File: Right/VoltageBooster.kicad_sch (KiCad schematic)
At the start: 5 parts, among them U32 BL8530_501SM

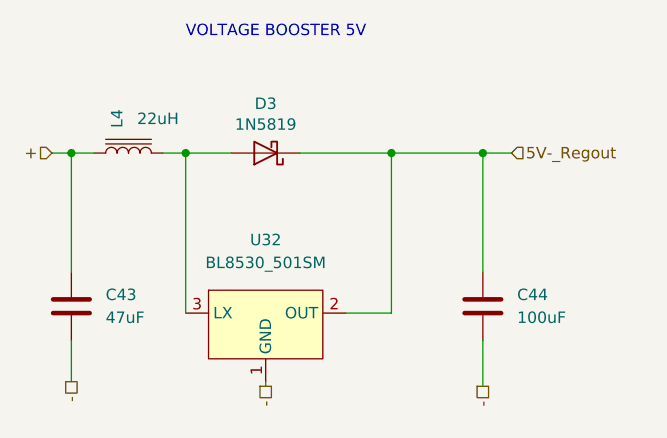
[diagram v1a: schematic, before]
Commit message: upgraded files to kicad7
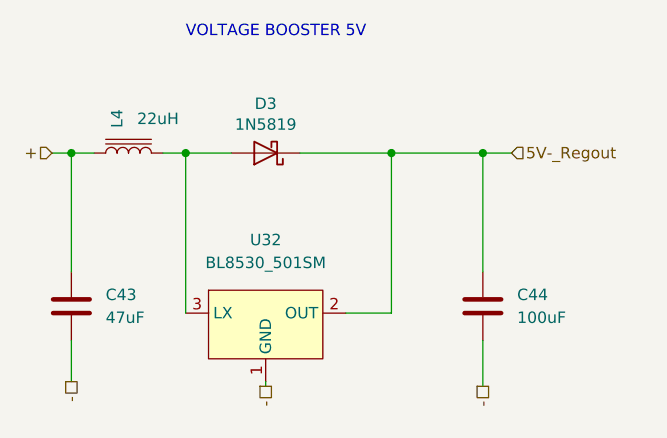
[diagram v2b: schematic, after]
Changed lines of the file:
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@@
-(kicad_sch (version 20211123) (generator eeschema)
+(kicad_sch (version 20230121) (generator eeschema)
   (paper "A4")
   (junction (at 121.158 95.504) (diameter 0) (color 0 0 0 0)
@@
   )
   (wire (pts (xy 154.178 121.412) (xy 154.178 116.332))
-    (stroke (width 0) (type default) (color 0 0 0 0))
+    (stroke (width 0) (type default))
   )
   (wire (pts (xy 121.158 95.504) (xy 126.238 95.504))
-    (stroke (width 0) (type default) (color 0 0 0 0))
+    (stroke (width 0) (type default))
   )
   (wire (pts (xy 108.458 95.504) (xy 110.998 95.504))
-    (stroke (width 0) (type default) (color 0 0 0 0))
+    (stroke (width 0) (type default))
   )
   (wire (pts (xy 154.178 95.504) (xy 144.018 95.504))
-    (stroke (width 0) (type default) (color 0 0 0 0))
+    (stroke (width 0) (type default))
   )
   (wire (pts (xy 106.299 95.504) (xy 108.458 95.504))
-    (stroke (width 0) (type default) (color 0 0 0 0))
+    (stroke (width 0) (type default))
   )
   (wire (pts (xy 144.018 113.284) (xy 144.018 95.504))
-    (stroke (width 0) (type default) (color 0 0 0 0))
+    (stroke (width 0) (type default))
   )
   (wire (pts (xy 108.458 95.504) (xy 108.458 108.712))
-    (stroke (width 0) (type default) (color 0 0 0 0))
+    (stroke (width 0) (type default))
   )
   (wire (pts (xy 154.178 95.504) (xy 154.178 108.712))
-    (stroke (width 0) (type default) (color 0 0 0 0))
+    (stroke (width 0) (type default))
   )
   (wire (pts (xy 130.048 121.412) (xy 130.048 120.904))
-    (stroke (width 0) (type default) (color 0 0 0 0))
+    (stroke (width 0) (type default))
   )
   (wire (pts (xy 144.018 95.504) (xy 133.858 95.504))
-    (stroke (width 0) (type default) (color 0 0 0 0))
+    (stroke (width 0) (type default))
   )
   (wire (pts (xy 154.178 95.504) (xy 157.353 95.504))
-    (stroke (width 0) (type default) (color 0 0 0 0))
+    (stroke (width 0) (type default))
   )
   (wire (pts (xy 118.618 95.504) (xy 121.158 95.504))
-    (stroke (width 0) (type default) (color 0 0 0 0))
+    (stroke (width 0) (type default))
   )
   (wire (pts (xy 138.938 113.284) (xy 144.018 113.284))
-    (stroke (width 0) (type default) (color 0 0 0 0))
+    (stroke (width 0) (type default))
   )
   (wire (pts (xy 121.158 95.504) (xy 121.158 113.284))
-    (stroke (width 0) (type default) (color 0 0 0 0))
+    (stroke (width 0) (type default))
   )
   (wire (pts (xy 108.458 120.904) (xy 108.458 116.332))
-    (stroke (width 0) (type default) (color 0 0 0 0))
+    (stroke (width 0) (type default))
   )
   (text "VOLTAGE BOOSTER 5V" (at 121.158 82.804 0)
     (effects (font (size 1.27 1.27)) (justify left bottom))
   )
-  (hierarchical_label "-" (shape passive) (at 130.048 121.412 270)
+  (hierarchical_label "-" (shape passive) (at 130.048 121.412 270) (fields_autoplaced)
     (effects (font (size 1.27 1.27)) (justify right))
   )
-  (hierarchical_label "-" (shape passive) (at 154.178 121.412 270)
+  (hierarchical_label "-" (shape passive) (at 154.178 121.412 270) (fields_autoplaced)
     (effects (font (size 1.27 1.27)) (justify right))
   )
-  (hierarchical_label "-" (shape passive) (at 108.458 120.904 270)
+  (hierarchical_label "-" (shape passive) (at 108.458 120.904 270) (fields_autoplaced)
     (effects (font (size 1.27 1.27)) (justify right))
   )
-  (hierarchical_label "+" (shape input) (at 106.299 95.504 180)
+  (hierarchical_label "+" (shape input) (at 106.299 95.504 180) (fields_autoplaced)
     (effects (font (size 1.27 1.27)) (justify right))
   )
-  (hierarchical_label "5V­_Regout" (shape input) (at 157.353 95.504 0)
+  (hierarchical_label "5V­_Regout" (shape input) (at 157.353 95.504 0) (fields_autoplaced)
     (effects (font (size 1.27 1.27)) (justify left))
   )
   (symbol (lib_id "Device:C") (at 108.458 112.522 0) (unit 1)
-    (in_bom yes) (on_board yes) (fields_autoplaced)
-    (property "Reference" "C43" (id 0) (at 112.268 111.2519 0)
+    (in_bom yes) (on_board yes) (dnp no) (fields_autoplaced)
+    (property "Reference" "C43" (at 112.268 111.2519 0)
       (effects (font (size 1.27 1.27)) (justify left))
     )
-    (property "Value" "47uF" (id 1) (at 112.268 113.7919 0)
+    (property "Value" "47uF" (at 112.268 113.7919 0)
       (effects (font (size 1.27 1.27)) (justify left))
     )
-    (property "Footprint" "Capacitor_SMD:C_0603_1608Metric" (id 2) (at 109.4232 116.332 0)
+    (property "Footprint" "Capacitor_SMD:C_0603_1608Metric" (at 109.4232 116.332 0)
       (effects (font (size 1.27 1.27)) hide)
     )
-    (property "Datasheet" "~" (id 3) (at 108.458 112.522 0)
+    (property "Datasheet" "~" (at 108.458 112.522 0)
       (effects (font (size 1.27 1.27)) hide)
     )
     (pin "1")
     (pin "2")
+    (instances
+      (project "Right"
+        (path "/94899d91-c8b6-48a0-9eee-db2609092a2a/1f805e46-8f6d-469f-a3f6-c7782bc31295"
+          (reference "C43") (unit 1)
+        )
+      )
+    )
   )
   (symbol (lib_id "Device:C") (at 154.178 112.522 0) (unit 1)
-    (in_bom yes) (on_board yes) (fields_autoplaced)
-    (property "Reference" "C44" (id 0) (at 157.988 111.2519 0)
+    (in_bom yes) (on_board yes) (dnp no) (fields_autoplaced)
+    (property "Reference" "C44" (at 157.988 111.2519 0)
       (effects (font (size 1.27 1.27)) (justify left))
     )
-    (property "Value" "100uF" (id 1) (at 157.988 113.7919 0)
+    (property "Value" "100uF" (at 157.988 113.7919 0)
       (effects (font (size 1.27 1.27)) (justify left))
     )
-    (property "Footprint" "Capacitor_SMD:C_1206_3216Metric" (id 2) (at 155.1432 116.332 0)
+    (property "Footprint" "Capacitor_SMD:C_1206_3216Metric" (at 155.1432 116.332 0)
       (effects (font (size 1.27 1.27)) hide)
     )
-    (property "Datasheet" "~" (id 3) (at 154.178 112.522 0)
+    (property "Datasheet" "~" (at 154.178 112.522 0)
       (effects (font (size 1.27 1.27)) hide)
     )
     (pin "1")
     (pin "2")
+    (instances
+      (project "Right"
+        (path "/94899d91-c8b6-48a0-9eee-db2609092a2a/1f805e46-8f6d-469f-a3f6-c7782bc31295"
+          (reference "C44") (unit 1)
+        )
+      )
+    )
   )
   (symbol (lib_id "Device:L_Iron") (at 114.808 95.504 90) (unit 1)
-    (in_bom yes) (on_board yes)
-    (property "Reference" "L4" (id 0) (at 113.5379 92.71 0)
+    (in_bom yes) (on_board yes) (dnp no)
+    (property "Reference" "L4" (at 113.5379 92.71 0)
       (effects (font (size 1.27 1.27)) (justify left))
     )
-    (property "Value" "22uH" (id 1) (at 120.396 91.694 90)
+    (property "Value" "22uH" (at 120.396 91.694 90)
       (effects (font (size 1.27 1.27)) (justify left))
     )
-    (property "Footprint" "Inductor_SMD:L_Taiyo-Yuden_NR-40xx" (id 2) (at 114.808 95.504 0)
+    (property "Footprint" "Inductor_SMD:L_Taiyo-Yuden_NR-40xx" (at 114.808 95.504 0)
       (effects (font (size 1.27 1.27)) hide)
     )
-    (property "Datasheet" "~" (id 3) (at 114.808 95.504 0)
+    (property "Datasheet" "~" (at 114.808 95.504 0)
       (effects (font (size 1.27 1.27)) hide)
     )
     (pin "1")
     (pin "2")
+    (instances
+      (project "Right"
+        (path "/94899d91-c8b6-48a0-9eee-db2609092a2a/1f805e46-8f6d-469f-a3f6-c7782bc31295"
+          (reference "L4") (unit 1)
+        )
+      )
+    )
   )
   (symbol (lib_id "Library:BL8530_501SM") (at 130.048 115.824 0) (unit 1)
-    (in_bom yes) (on_board yes) (fields_autoplaced)
-    (property "Reference" "U32" (id 0) (at 130.048 105.156 0))
-    (property "Value" "BL8530_501SM" (id 1) (at 130.048 107.696 0))
-    (property "Footprint" "Package_TO_SOT_SMD:SOT-89-3" (id 2) (at 128.778 108.204 0)
+    (in_bom yes) (on_board yes) (dnp no) (fields_autoplaced)
+    (property "Reference" "U32" (at 130.048 105.156 0)
+      (effects (font (size 1.27 1.27)))
+    )
+    (property "Value" "BL8530_501SM" (at 130.048 107.696 0)
+      (effects (font (size 1.27 1.27)))
+    )
+    (property "Footprint" "Package_TO_SOT_SMD:SOT-89-3" (at 128.778 108.204 0)
       (effects (font (size 1.27 1.27)) hide)
     )
-    (property "Datasheet" "" (id 3) (at 128.778 108.204 0)
+    (property "Datasheet" "" (at 128.778 108.204 0)
       (effects (font (size 1.27 1.27)) hide)
     )
@@
     (pin "2")
     (pin "3")
+    (instances
+      (project "Right"
+        (path "/94899d91-c8b6-48a0-9eee-db2609092a2a/1f805e46-8f6d-469f-a3f6-c7782bc31295"
+          (reference "U32") (unit 1)
+        )
+      )
+    )
   )
   (symbol (lib_id "nrfmicro-rescue:MBR0520") (at 130.048 95.504 180) (unit 1)
-    (in_bom yes) (on_board yes)
-    (property "Reference" "D3" (id 0) (at 130.048 90.0176 0))
-    (property "Value" "1N5819" (id 1) (at 130.048 92.329 0))
-    (property "Footprint" "Diode_SMD:D_SOD-323F" (id 2) (at 130.048 91.059 0)
+    (in_bom yes) (on_board yes) (dnp no)
+    (property "Reference" "D3" (at 130.048 90.0176 0)
+      (effects (font (size 1.27 1.27)))
+    )
+    (property "Value" "1N5819" (at 130.048 92.329 0)
+      (effects (font (size 1.27 1.27)))
+    )
+    (property "Footprint" "Diode_SMD:D_SOD-323F" (at 130.048 91.059 0)
       (effects (font (size 1.27 1.27)) hide)
     )
-    (property "Datasheet" "" (id 3) (at 130.048 95.504 0)
+    (property "Datasheet" "" (at 130.048 95.504 0)
       (effects (font (size 1.27 1.27)) hide)
     )
     (pin "1")
     (pin "2")
+    (instances
+      (project "Right"
+        (path "/94899d91-c8b6-48a0-9eee-db2609092a2a/1f805e46-8f6d-469f-a3f6-c7782bc31295"
+          (reference "D3") (unit 1)
+        )
+      )
+    )
   )
 )
